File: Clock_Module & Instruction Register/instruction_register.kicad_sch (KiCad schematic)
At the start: 22 parts, among them U12 74LS245, U13 74LS173, U14 74LS173

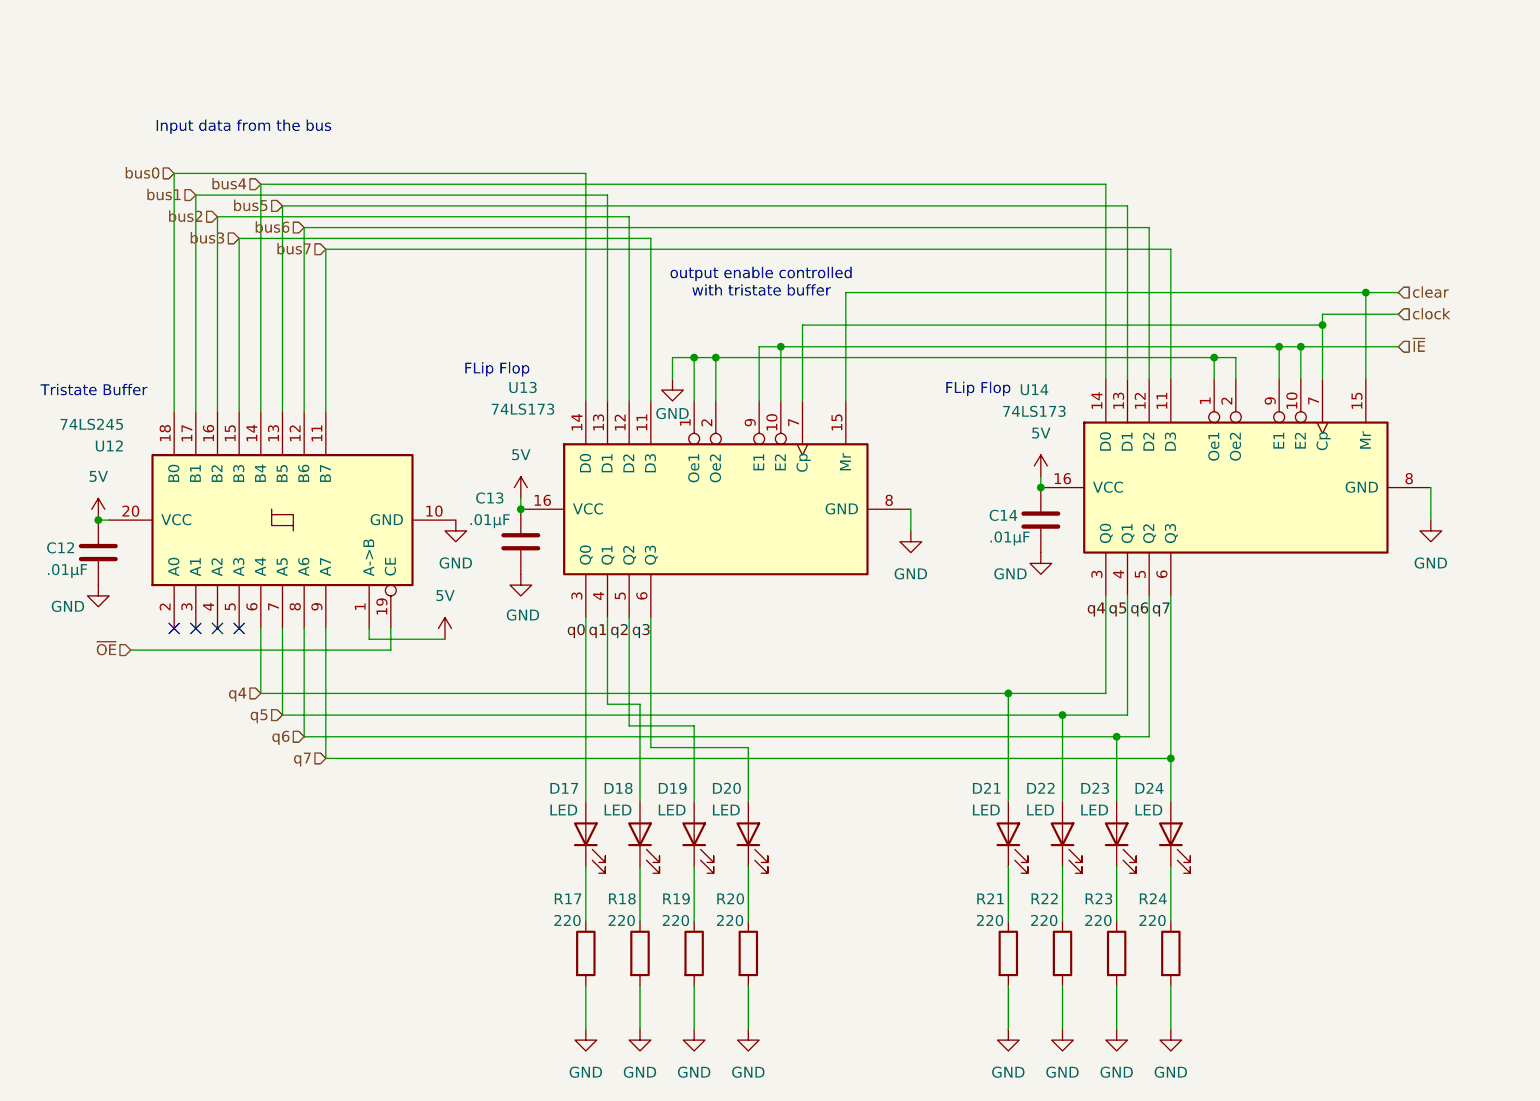
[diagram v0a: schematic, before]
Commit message: Placed clock module again
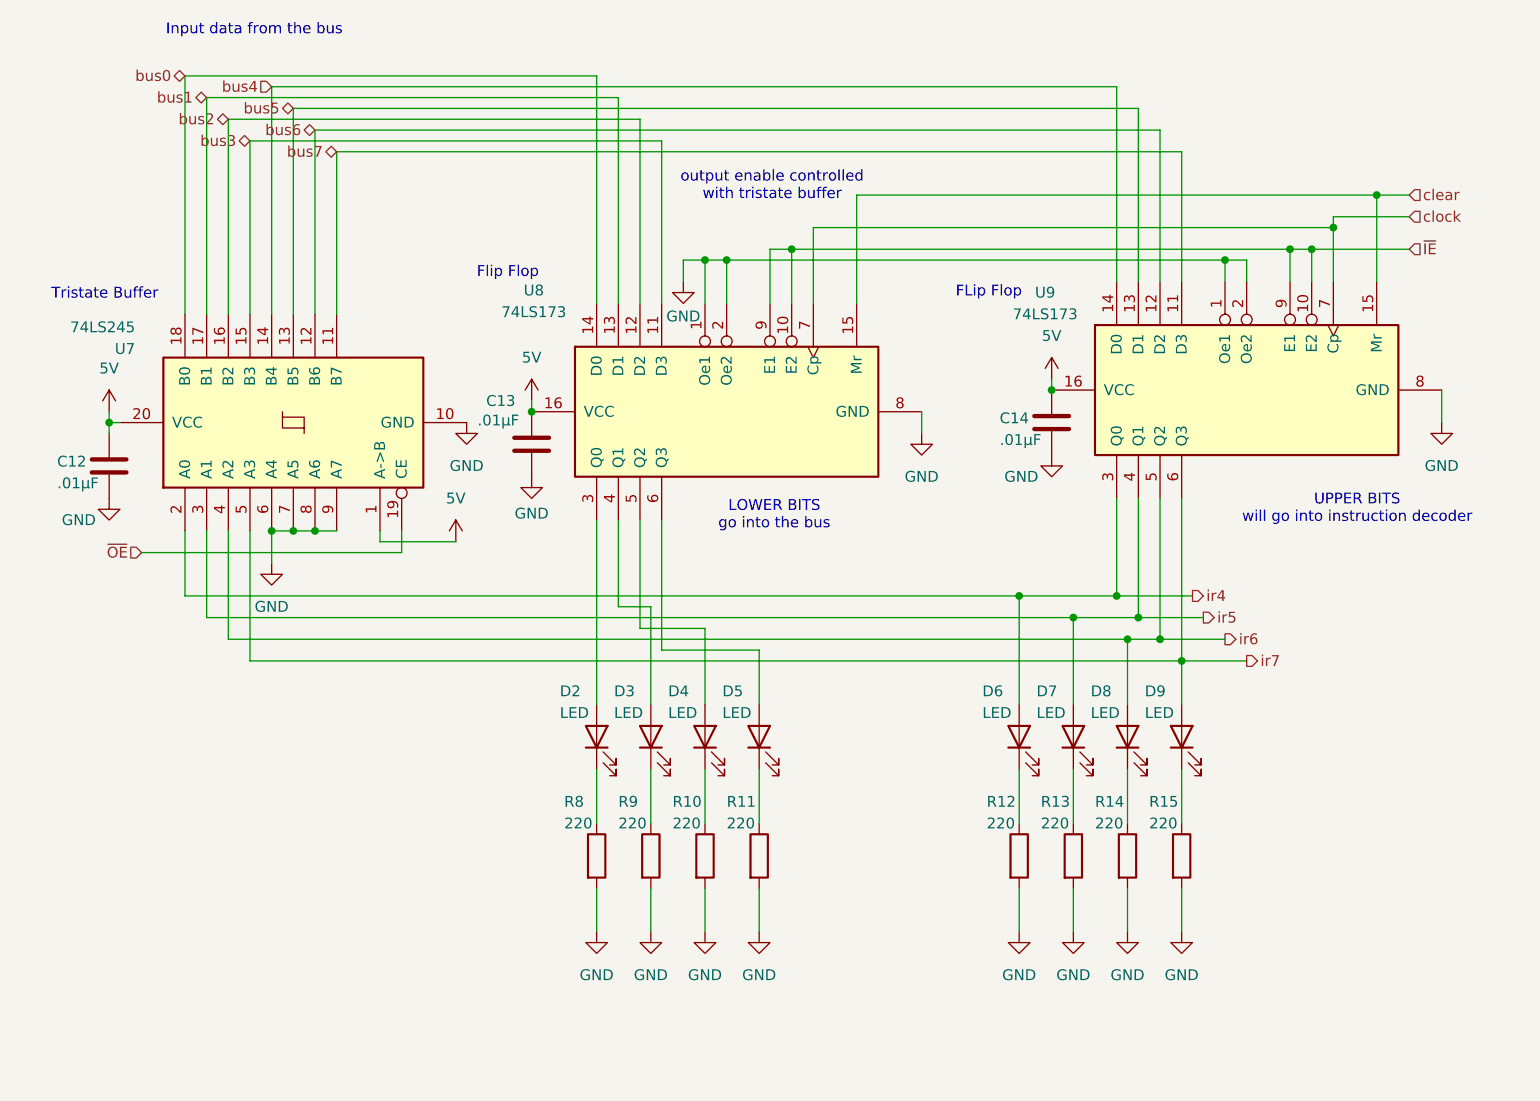
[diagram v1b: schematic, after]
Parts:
- removed D17, D18, D19, D20, D21, D22, D23, D24: LED, LED_THT:LED_D5.0mm, symbol Device:LED
- removed R17, R18, R19, R20, R21, R22, R23, R24: 220, Resistor_THT:R_Axial_DIN0207_L6.3mm_D2.5mm_P5.08mm_Vertical, symbol Device:R
- removed U12: 74LS245, Package_DIP:DIP-20_W7.62mm, symbol 74xx:74LS245
- removed U13, U14: 74LS173, Package_DIP:DIP-16_W7.62mm, symbol 74xx:74LS173
- added D2, D3, D4, D5, D6, D7, D8, D9: LED, LED_THT:LED_D5.0mm, symbol Device:LED
- added R10, R11, R12, R13, R14, R15, R8, R9: 220, Resistor_THT:R_Axial_DIN0207_L6.3mm_D2.5mm_P5.08mm_Vertical, symbol Device:R
- added U7: 74LS245, Package_DIP:DIP-20_W7.62mm, symbol 74xx:74LS245
- added U8, U9: 74LS173, Package_DIP:DIP-16_W7.62mm, symbol 74xx:74LS173
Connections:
- net 5V: now also U7.1 (A->B), U7.20 (VCC), U8.16 (VCC), U9.16 (VCC)
- net GND: now also R10.2, R11.2, R12.2, R13.2, R14.2, R15.2, R8.2, R9.2, U7.10 (GND), U7.6 (A4), U7.7 (A5), U7.8 (A6), U7.9 (A7), U8.1 (Oe1), U8.2 (Oe2), U8.8 (GND), U9.1 (Oe1), U9.2 (Oe2), U9.8 (GND)
- net bus0: now also U7.18 (B0), U8.14 (D0)
- net bus1: now also U7.17 (B1), U8.13 (D1)
- net bus2: now also U7.16 (B2), U8.12 (D2)
- net bus3: now also U7.15 (B3), U8.11 (D3)
- net bus4: now also U7.14 (B4), U9.14 (D0)
- net bus5: now also U7.13 (B5), U9.13 (D1)
- net bus6: now also U7.12 (B6), U9.12 (D2)
- net bus7: now also U7.11 (B7), U9.11 (D3)
- net clear: now also U8.15 (Mr), U9.15 (Mr)
- net clock: now also U8.7 (Cp), U9.7 (Cp)
- net ~{IE}: now also U8.10 (E2), U8.9 (E1), U9.10 (E2), U9.9 (E1)
- net ~{OE}: now also U7.19 (CE)
- new net: D7.1 (K), R13.1
- new net: D3.1 (K), R9.1
- new net: D3.2 (A), U8.4 (Q1)
- new net: D6.1 (K), R12.1
- new net: D4.1 (K), R10.1
- new net: D4.2 (A), U8.5 (Q2)
- new net: D5.1 (K), R11.1
- new net: D9.1 (K), R15.1
- new net: D8.1 (K), R14.1
- new net: D5.2 (A), U8.6 (Q3)
- new net: D2.1 (K), R8.1
- new net: D2.2 (A), U8.3 (Q0)
- new net ir4: D6.2 (A), U7.2 (A0), U9.3 (Q0)
- new net ir5: D7.2 (A), U7.3 (A1), U9.4 (Q1)
- new net ir6: D8.2 (A), U7.4 (A2), U9.5 (Q2)
- new net ir7: D9.2 (A), U7.5 (A3), U9.6 (Q3)
- no-connect marks 4 -> 0
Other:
- note added: "Flip Flop"
- note added: "LOWER BITS go into the bus"
- note added: "UPPER BITS will go into instruction decoder"
- company: Arsenal Gear -> (none)
